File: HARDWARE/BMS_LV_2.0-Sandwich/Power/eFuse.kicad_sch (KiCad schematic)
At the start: 13 parts, among them Q10 BSS138, Q12 SIR5607DP-T1-RE3, Q13 SIR5607DP-T1-RE3, Q14 SIR5607DP-T1-RE3, Q15 SIR5607DP-T1-RE3

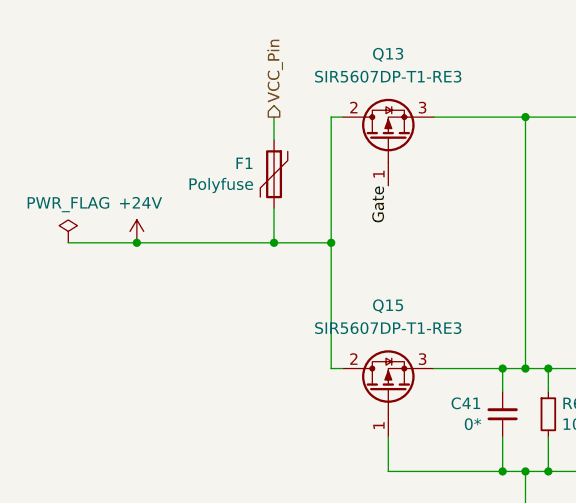
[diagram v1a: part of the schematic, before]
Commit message: Naprawiono: załączanie lv, brak zlącza programatora (XD) oraz brak podłączenia czujnika prądu :9
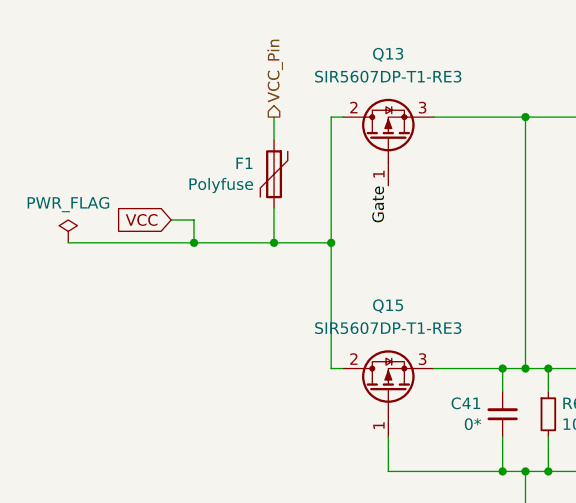
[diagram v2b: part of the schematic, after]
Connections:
- net +24V renamed VCC
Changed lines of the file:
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@@
-	)
-	(junction
-		(at 107.95 71.12)
-		(diameter 0)
-		(color 0 0 0 0)
 	)
 	(junction
@@
 	)
 	(junction
+		(at 114.3 71.12)
+		(diameter 0)
+		(color 0 0 0 0)
+	)
+	(junction
 		(at 180.34 81.28)
 		(diameter 0)
@@
 	(wire
 		(pts
-			(xy 107.95 71.12) (xy 123.19 71.12)
+			(xy 100.33 71.12) (xy 114.3 71.12)
 		)
 		(stroke
@@
 	(wire
 		(pts
+			(xy 114.3 68.58) (xy 114.3 71.12)
+		)
+		(stroke
+			(width 0)
+			(type default)
+		)
+	)
+	(wire
+		(pts
 			(xy 153.67 92.71) (xy 153.67 96.52)
 		)
@@
 	(wire
 		(pts
-			(xy 107.95 71.12) (xy 100.33 71.12)
+			(xy 114.3 71.12) (xy 123.19 71.12)
 		)
 		(stroke
@@
 		(pts
 			(xy 151.13 57.15) (xy 161.29 57.15)
+		)
+		(stroke
+			(width 0)
+			(type default)
+		)
+	)
+	(wire
+		(pts
+			(xy 111.76 68.58) (xy 114.3 68.58)
 		)
 		(stroke
@@
 			)
 			(justify right bottom)
+		)
+	)
+	(global_label "VCC"
+		(shape input)
+		(at 111.76 68.58 180)
+		(fields_autoplaced yes)
+		(effects
+			(font
+				(size 1.27 1.27)
+			)
+			(justify right)
+		)
+		(property "Intersheetrefs" "${INTERSHEET_REFS}"
+			(at 105.8004 68.58 0)
+			(hide yes)
+			(show_name no)
+			(do_not_autoplace no)
+			(effects
+				(font
+					(size 1.27 1.27)
+				)
+				(justify right)
+			)
 		)
 	)
@@
 					(unit 1)
 				)
-			)
-		)
-	)
-	(symbol
-		(lib_id "BMS_LV_2022-rescue:+24V-power")
-		(at 107.95 71.12 0)
-		(unit 1)
-		(body_style 1)
-		(exclude_from_sim no)
-		(in_bom yes)
-		(on_board yes)
-		(in_pos_files yes)
-		(dnp no)
-		(property "Reference" "#PWR047"
-			(at 107.95 74.93 0)
-			(hide yes)
-			(show_name no)
-			(do_not_autoplace no)
-			(effects
-				(font
-					(size 1.27 1.27)
-				)
-			)
-		)
-		(property "Value" "+24V"
-			(at 108.331 66.7258 0)
-			(show_name no)
-			(do_not_autoplace no)
-			(effects
-				(font
-					(size 1.27 1.27)
-				)
-			)
-		)
-		(property "Footprint" ""
-			(at 107.95 71.12 0)
-			(hide yes)
-			(show_name no)
-			(do_not_autoplace no)
-			(effects
-				(font
-					(size 1.27 1.27)
-				)
-			)
-		)
-		(property "Datasheet" ""
-			(at 107.95 71.12 0)
-			(hide yes)
-			(show_name no)
-			(do_not_autoplace no)
-			(effects
-				(font
-					(size 1.27 1.27)
-				)
-			)
-		)
-		(property "Description" ""
-			(at 107.95 71.12 0)
-			(hide yes)
-			(show_name no)
-			(do_not_autoplace no)
-			(effects
-				(font
-					(size 1.27 1.27)
-				)
-			)
-		)
-		(pin "1"
-		)
-		(instances
-			(project "BMS_LV_2022"
-				(path "/fb6504b5-591d-4b10-ab86-0c46f59e8b7d/00000000-0000-0000-0000-00006269845f"
-					(reference "#PWR047")
-					(unit 1)
-				)

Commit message: Poprawki , tvs , programator
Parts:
- Q12, Q13, Q14, Q15: symbol Transistor_FET:Q_PMOS_GDS -> Transistor_FET:Q_PMOS_GSD
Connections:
- net CurrentSensor_IP+: now also Q12.3 (D), Q14.3 (D); no longer Q12.2 (D), Q14.2 (D)
- net VCC: now also Q13.3 (D), Q15.3 (D); no longer Q13.2 (D), Q15.2 (D)
- new net: C41.2, Q12.2 (S), Q13.2 (S), Q14.2 (S), Q15.2 (S), R62.1
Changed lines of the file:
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@@
 	)
 	(symbol
-		(lib_id "Transistor_FET:Q_PMOS_GDS")
+		(lib_id "Transistor_FET:Q_PMOS_GSD")
 		(at 166.37 59.69 270)
 		(mirror x)
@@
 				(font
 					(size 1.27 1.27)
-					(italic yes)
-				)
-				(justify left)
+				)
 			)
 		)
@@
 					(size 1.27 1.27)
 				)
-				(justify right)
-			)
-		)
-		(property "Description" ""
+			)
+		)
+		(property "Description" "P-MOSFET transistor, gate/source/drain"
 			(at 166.37 59.69 0)
 			(hide yes)
@@
 	)
 	(symbol
-		(lib_id "Transistor_FET:Q_PMOS_GDS")
+		(lib_id "Transistor_FET:Q_PMOS_GSD")
 		(at 135.89 87.63 90)
 		(unit 1)
@@
 		(fields_autoplaced yes)
 		(property "Reference" "Q15"
-			(at 135.89 78.105 90)
+			(at 135.89 78.74 90)
 			(show_name no)
 			(do_not_autoplace no)
@@
 		)
 		(property "Value" "SIR5607DP-T1-RE3"
-			(at 135.89 80.645 90)
+			(at 135.89 81.28 90)
 			(show_name no)
 			(do_not_autoplace no)
@@
 				(font
 					(size 1.27 1.27)
-					(italic yes)
-				)
-				(justify left)
+				)
 			)
 		)
@@
 					(size 1.27 1.27)
 				)
-				(justify right)
-			)
-		)
-		(property "Description" ""
+			)
+		)
+		(property "Description" "P-MOSFET transistor, gate/source/drain"
 			(at 135.89 87.63 0)
 			(hide yes)
@@
 	)
 	(symbol
-		(lib_id "Transistor_FET:Q_PMOS_GDS")
+		(lib_id "Transistor_FET:Q_PMOS_GSD")
 		(at 135.89 59.69 90)
 		(unit 1)
@@
 		(fields_autoplaced yes)
 		(property "Reference" "Q13"
-			(at 135.89 50.165 90)
+			(at 135.89 50.8 90)
 			(show_name no)
 			(do_not_autoplace no)
@@
 		)
 		(property "Value" "SIR5607DP-T1-RE3"
-			(at 135.89 52.705 90)
+			(at 135.89 53.34 90)
 			(show_name no)
 			(do_not_autoplace no)
@@
 				(font
 					(size 1.27 1.27)
-					(italic yes)
-				)
-				(justify left)
+				)
 			)
 		)
@@
 					(size 1.27 1.27)
 				)
-				(justify right)
-			)
-		)
-		(property "Description" ""
+			)
+		)
+		(property "Description" "P-MOSFET transistor, gate/source/drain"
 			(at 135.89 59.69 0)
 			(hide yes)
@@
 	)
 	(symbol
-		(lib_id "Transistor_FET:Q_PMOS_GDS")
+		(lib_id "Transistor_FET:Q_PMOS_GSD")
 		(at 166.37 87.63 270)
 		(mirror x)
@@
 				(font
 					(size 1.27 1.27)
-					(italic yes)
-				)
-				(justify left)
+				)
 			)
 		)
@@
 					(size 1.27 1.27)
 				)
-				(justify right)
-			)
-		)
-		(property "Description" ""
+			)
+		)
+		(property "Description" "P-MOSFET transistor, gate/source/drain"
 			(at 166.37 87.63 0)
 			(hide yes)
